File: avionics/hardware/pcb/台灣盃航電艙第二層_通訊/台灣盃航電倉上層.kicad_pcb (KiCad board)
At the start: 4 copper layers, 80 x 80 mm, 39 parts, among them J1 SMA, U1 LIS3MDL, U2 NEO-M9N, U3 E22-900T22S, U4 Connector

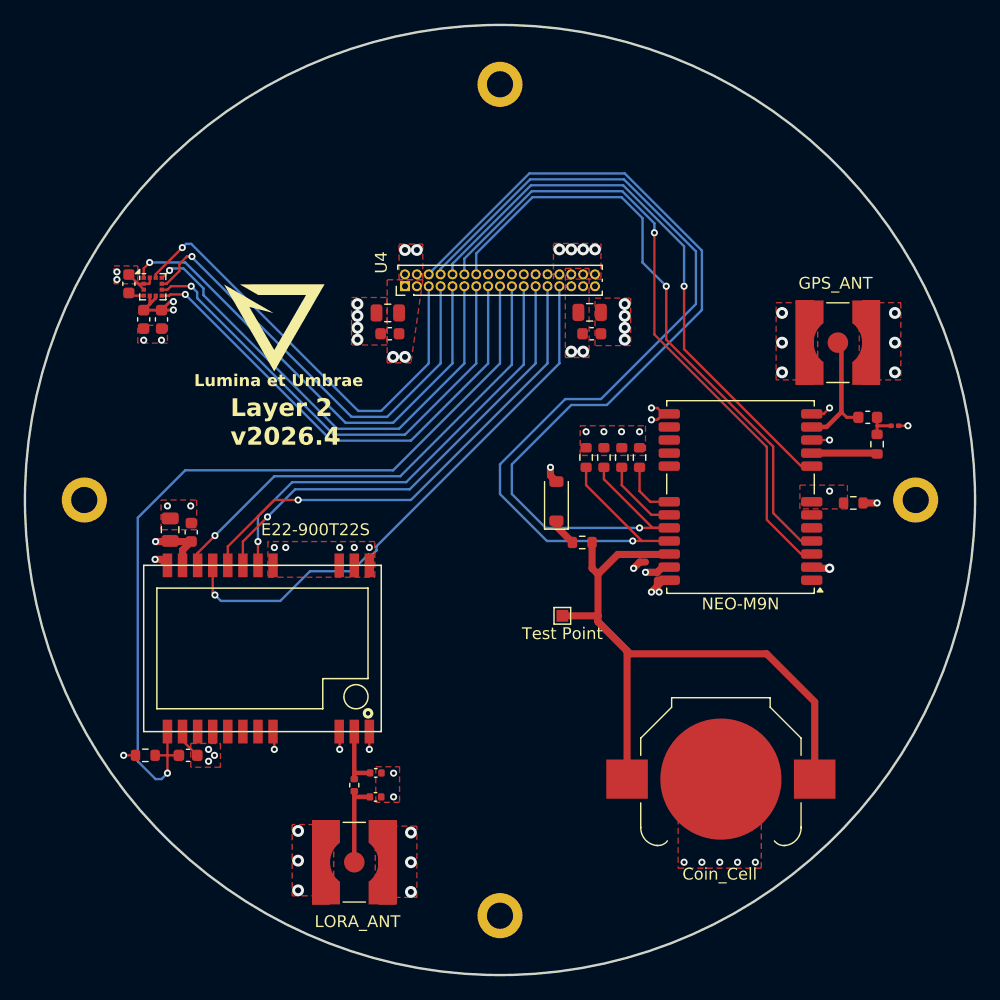
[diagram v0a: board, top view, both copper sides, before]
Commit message: 上傳新的連接器
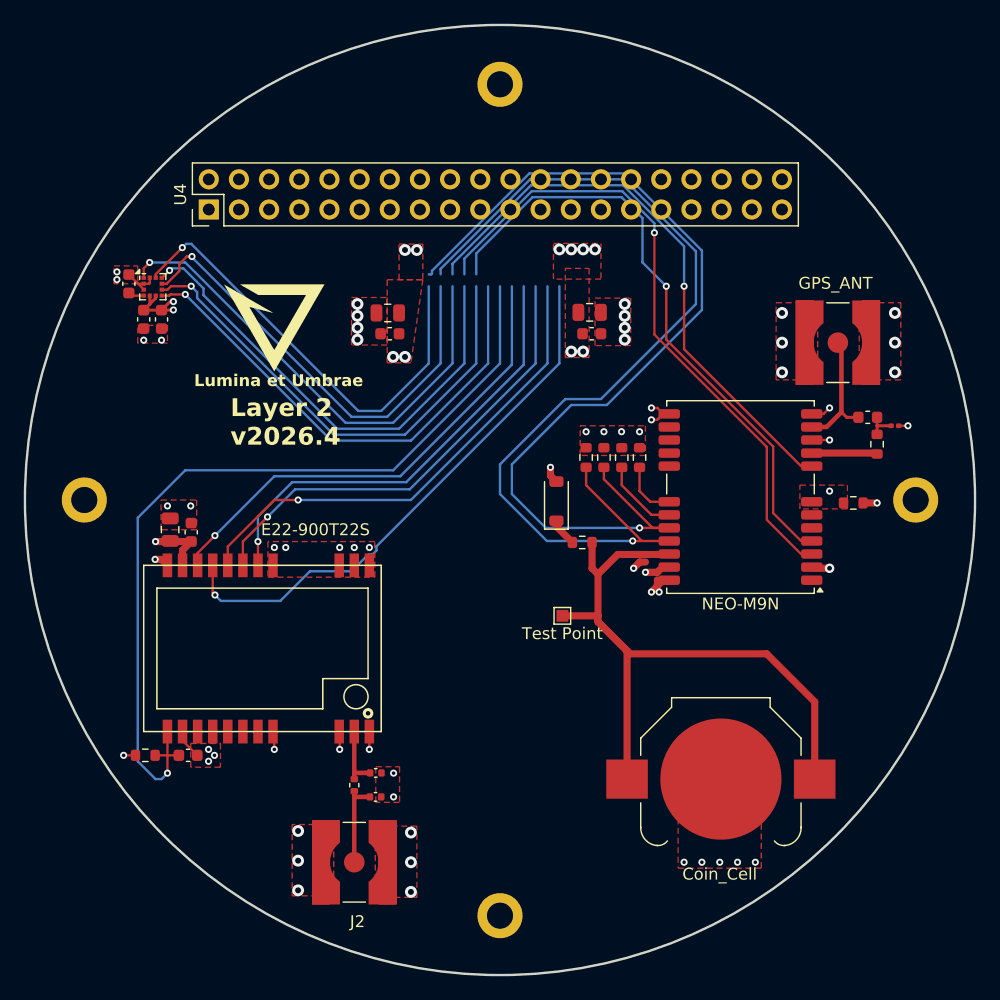
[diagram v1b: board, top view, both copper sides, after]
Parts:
- U4: footprint Connector_PinHeader_1.00mm:PinHeader_2x17_P1.00mm_Vertical -> Connector_PinHeader_2.54mm:PinHeader_2x20_P2.54mm_Vertical
- moved U4 17.7 mm to (122.5, 71.5)
- renumbered LORA_ANT to J2

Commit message: 將第一至三層連接器修改成PC104規格，第四層還未進行
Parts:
- removed C10, C11: 100n, Capacitor_SMD:C_0603_1608Metric
- removed C7, C8: 10u, Capacitor_SMD:C_0805_2012Metric
- removed U4: Connector, Connector_PinHeader_2.54mm:PinHeader_2x20_P2.54mm_Vertical
- added C22: 100n, Capacitor_SMD:C_0402_1005Metric, B.Cu at (118.8, 71.9)
- added C23: 10u, Capacitor_SMD:C_0603_1608Metric, B.Cu at (120.0, 72.2)
- added C24: 100n, Capacitor_SMD:C_0402_1005Metric, B.Cu at (174.5, 72.0)
- added C25: 10u, Capacitor_SMD:C_0603_1608Metric, B.Cu at (173.2, 72.2)
- added U5: Connector, Connector_PinHeader_2.54mm:PinHeader_2x20_P2.54mm_Vertical, F.Cu at (122.5, 71.0)
- moved C2 4.73 mm to (115.2, 82.5)
- moved C3 4.73 mm to (116.5, 85.5)
- moved C4 4.73 mm to (118.0, 85.5)
- moved U1 4.73 mm to (117.3, 82.8)
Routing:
- net GPS_TX: track 80.4 -> 57.7 mm, vias 1 -> 3
- net GPS_RX: track 81.2 -> 58.5 mm, vias 1 -> 3
- net SPI2_MOSI: track 38.3 -> 17.3 mm, vias 1 -> 0
- net SPI2_MISO: track 38.8 -> 19.9 mm, vias 1 -> 0
- net SPI2_SCK: track 41.2 -> 23.7 mm, vias 1 -> 2
- net CS_MAG: track 40.5 -> 24.3 mm, vias 1 -> 2
- net DRDY_MAG: track 41.1 -> 27.2 mm, vias 1 -> 0
- net INT_MAG: track 41.8 -> 30.0 mm, vias 1 -> 0
- net LORA_TX: track 46.8 -> 56.3 mm
- net LORA_RX: track 41.4 -> 50.3 mm
- net LORA_M1: track 39.4 -> 47.6 mm
- net LORA_M0: track 38.4 -> 46.0 mm
- net LORA_AUX: track 40.7 -> 47.6 mm
- net LORA_RESET: track 71.7 -> 78.1 mm
- net INT_GPS: track 52.1 -> 47.1 mm, vias 1 -> 0
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- added copper zone on B.Cu, net +3V3
- added copper zone on B.Cu, net GND
